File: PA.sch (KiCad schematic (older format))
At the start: 34 parts, among them IC1 CC1190

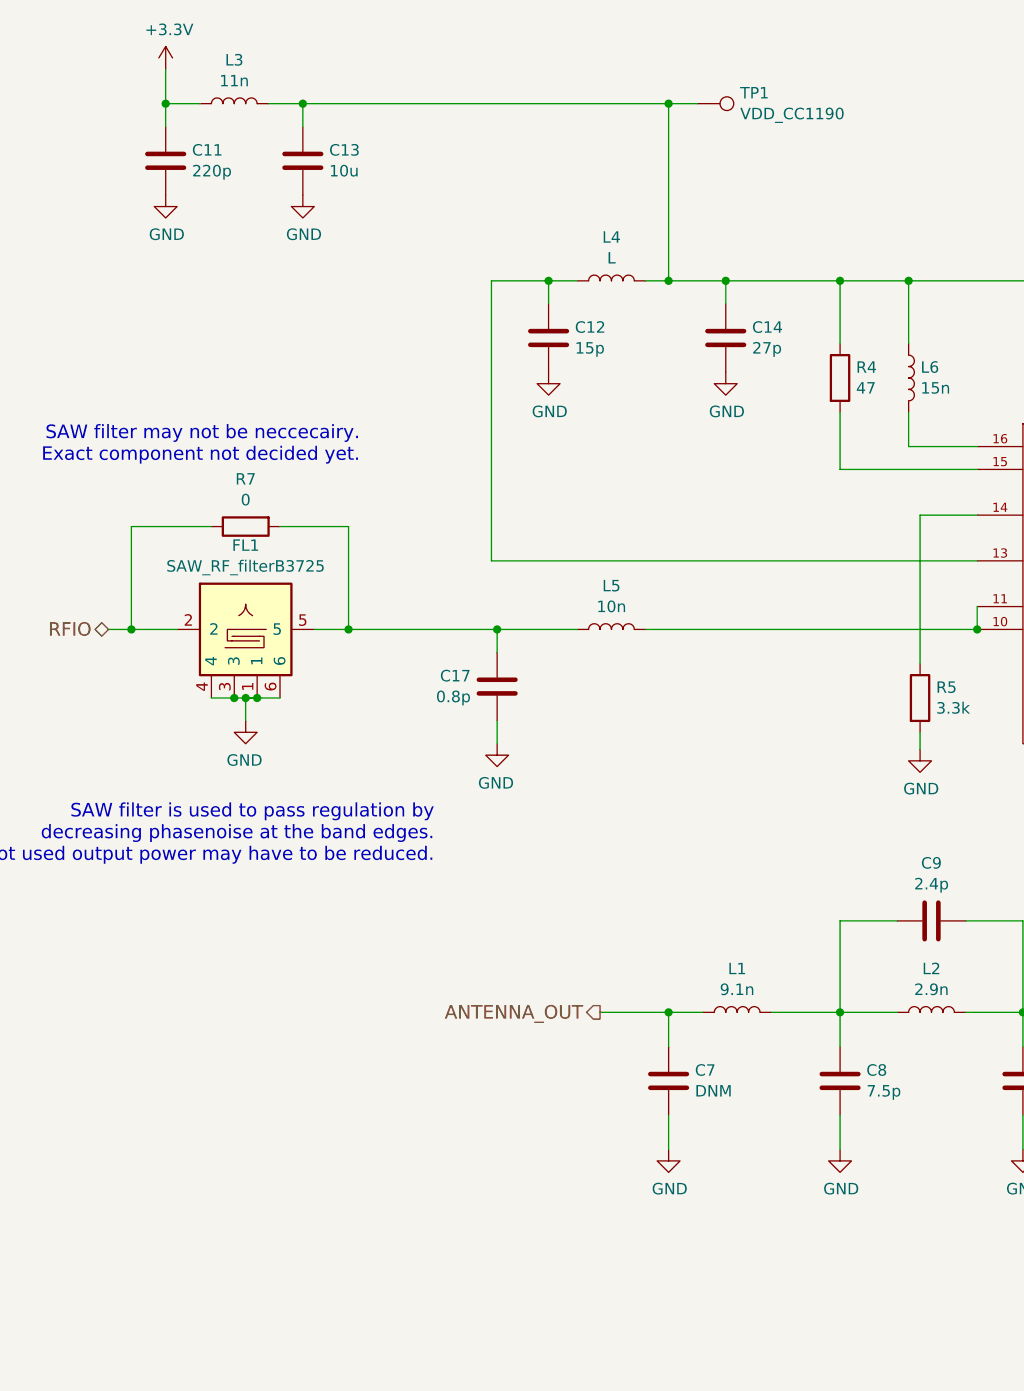
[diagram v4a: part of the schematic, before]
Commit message: Routed power for RF
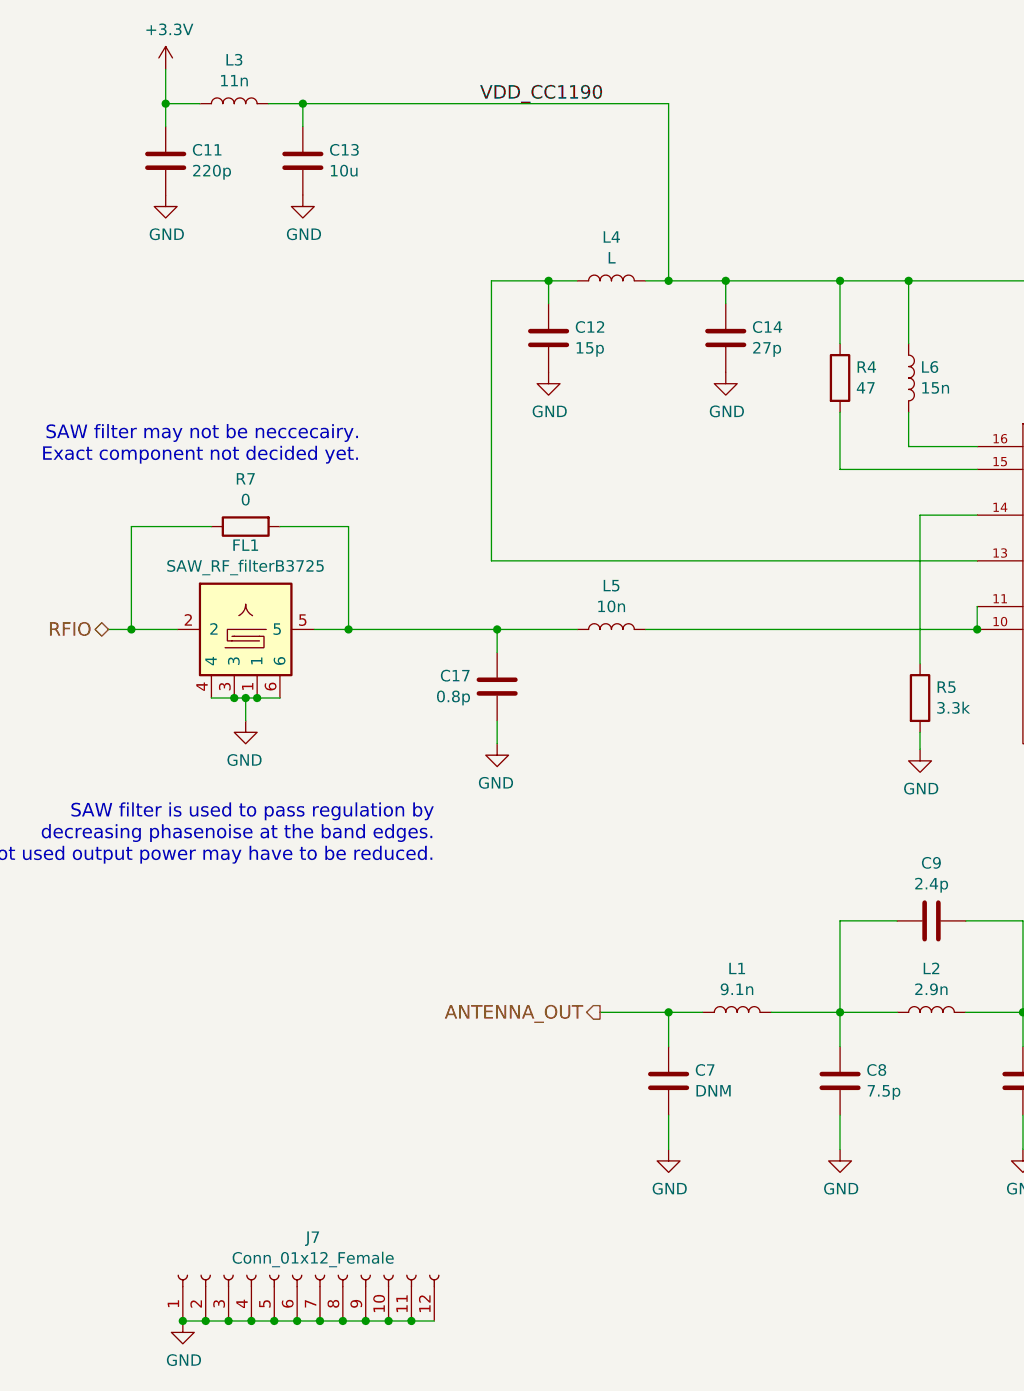
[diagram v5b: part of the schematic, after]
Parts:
- removed TP1: VDD_CC1190, TestPoint:TestPoint_Pad_2.0x2.0mm, symbol Connector:TestPoint
- added J7: Conn_01x12_Female, TU-HW RF LIB:BMIS202F, symbol Connector:Conn_01x12_Female
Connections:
- net GND: now also J7.1 (Pin_1), J7.10 (Pin_10), J7.11 (Pin_11), J7.12 (Pin_12), J7.2 (Pin_2), J7.3 (Pin_3), J7.4 (Pin_4), J7.5 (Pin_5), J7.6 (Pin_6), J7.7 (Pin_7), J7.8 (Pin_8), J7.9 (Pin_9)
- net VDD_CC1190: now reaches C13.1, C14.1, C40.1, C42.1, C43.1, L3.2, L4.2, L6.1, L8.1, R4.1
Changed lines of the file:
@@
 	6875 3700 6875 3425
-$Comp
-L Connector:TestPoint TP1
-U 1 1 601A7C22
-P 4125 975
-F 0 "TP1" V 4079 1163 50  0000 L CNN
-F 1 "VDD_CC1190" V 4170 1163 50  0000 L CNN
-F 2 "TestPoint:TestPoint_Pad_2.0x2.0mm" H 4325 975 50  0001 C CNN
-F 3 "~" H 4325 975 50  0001 C CNN
-	1    4125 975
-	0    1    1    0
-$EndComp
 $Comp
 L Device:C C11
@@
 Connection ~ 2400 975
 Wire Wire Line
-	4000 975  4125 975
-Wire Wire Line
 	4000 975  4000 1750
 Wire Wire Line
@@
 Wire Wire Line
 	2400 975  4000 975
-Connection ~ 4000 975
 Connection ~ 2150 3575
 Wire Wire Line
@@
 Wire Wire Line
 	2100 3575 2150 3575
-Wire Wire Line
-	2150 3575 2200 3575
 Connection ~ 2100 3575
 Connection ~ 2200 3575
 Wire Wire Line
 	2200 3575 2300 3575
+$Comp
+L power:GND #PWR0103
+U 1 1 602D8673
+P 1875 6300
+F 0 "#PWR0103" H 1875 6050 50  0001 C CNN
+F 1 "GND" H 1880 6127 50  0000 C CNN
+F 2 "" H 1875 6300 50  0001 C CNN
+F 3 "" H 1875 6300 50  0001 C CNN
+	1    1875 6300
+	1    0    0    -1
+$EndComp
+$Comp
+L Connector:Conn_01x12_Female J7
+U 1 1 602E7893
+P 2375 6100
+F 0 "J7" V 2540 6030 50  0000 C CNN
+F 1 "Conn_01x12_Female" V 2449 6030 50  0000 C CNN
+F 2 "TU-HW RF LIB:BMIS202F" H 2375 6100 50  0001 C CNN
+F 3 "~" H 2375 6100 50  0001 C CNN
+	1    2375 6100
+	0    -1   -1   0
+$EndComp
+Wire Wire Line
+	1875 6300 1975 6300
+Connection ~ 1875 6300
+Connection ~ 1975 6300
+Wire Wire Line
+	1975 6300 2075 6300
+Connection ~ 2075 6300
+Wire Wire Line
+	2075 6300 2175 6300
+Connection ~ 2175 6300
+Wire Wire Line
+	2175 6300 2275 6300
+Connection ~ 2275 6300
+Wire Wire Line
+	2275 6300 2375 6300
+Connection ~ 2375 6300
+Wire Wire Line
+	2375 6300 2475 6300
+Connection ~ 2475 6300
+Wire Wire Line
+	2475 6300 2575 6300
+Connection ~ 2575 6300
+Wire Wire Line
+	2575 6300 2675 6300
+Connection ~ 2675 6300
+Wire Wire Line
+	2675 6300 2775 6300
+Connection ~ 2775 6300
+Wire Wire Line
+	2775 6300 2875 6300
+Connection ~ 2875 6300
+Wire Wire Line
+	2875 6300 2975 6300
+Text Label 3175 975  0    59   ~ 0
+VDD_CC1190
 $EndSCHEMATC

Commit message: Feedback from peer review
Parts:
- removed J7: Conn_01x12_Female, TU-HW RF LIB:BMIS202F, symbol Connector:Conn_01x12_Female
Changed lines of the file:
@@
 Wire Wire Line
 	2200 3575 2300 3575
-$Comp
-L power:GND #PWR0103
-U 1 1 602D8673
-P 1875 6300
-F 0 "#PWR0103" H 1875 6050 50  0001 C CNN
-F 1 "GND" H 1880 6127 50  0000 C CNN
-F 2 "" H 1875 6300 50  0001 C CNN
-F 3 "" H 1875 6300 50  0001 C CNN
-	1    1875 6300
-	1    0    0    -1
-$EndComp
-$Comp
-L Connector:Conn_01x12_Female J7
-U 1 1 602E7893
-P 2375 6100
-F 0 "J7" V 2540 6030 50  0000 C CNN
-F 1 "Conn_01x12_Female" V 2449 6030 50  0000 C CNN
-F 2 "TU-HW RF LIB:BMIS202F" H 2375 6100 50  0001 C CNN
-F 3 "~" H 2375 6100 50  0001 C CNN
-	1    2375 6100
-	0    -1   -1   0
-$EndComp
-Wire Wire Line
-	1875 6300 1975 6300
-Connection ~ 1875 6300
-Connection ~ 1975 6300
-Wire Wire Line
-	1975 6300 2075 6300
-Connection ~ 2075 6300
-Wire Wire Line
-	2075 6300 2175 6300
-Connection ~ 2175 6300
-Wire Wire Line
-	2175 6300 2275 6300
-Connection ~ 2275 6300
-Wire Wire Line
-	2275 6300 2375 6300
-Connection ~ 2375 6300
-Wire Wire Line
-	2375 6300 2475 6300
-Connection ~ 2475 6300
-Wire Wire Line
-	2475 6300 2575 6300
-Connection ~ 2575 6300
-Wire Wire Line
-	2575 6300 2675 6300
-Connection ~ 2675 6300
-Wire Wire Line
-	2675 6300 2775 6300
-Connection ~ 2775 6300
-Wire Wire Line
-	2775 6300 2875 6300
-Connection ~ 2875 6300
-Wire Wire Line
-	2875 6300 2975 6300
 Text Label 3175 975  0    59   ~ 0
 VDD_CC1190

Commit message: Added PA shield
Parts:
- added J7: RF_Shield_One_Piece, TU-HW RF LIB:WE_shield_20x20_36503205S, symbol Device:RF_Shield_One_Piece
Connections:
- net GND: now also J7.1 (Shield)
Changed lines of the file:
@@
 Text Label 3175 975  0    59   ~ 0
 VDD_CC1190
+$Comp
+L Device:RF_Shield_One_Piece J7
+U 1 1 60330292
+P 4975 6825
+F 0 "J7" H 5605 6814 50  0000 L CNN
+F 1 "RF_Shield_One_Piece" H 5605 6723 50  0000 L CNN
+F 2 "TU-HW RF LIB:WE_shield_20x20_36503205S" H 4975 6725 50  0001 C CNN
+F 3 "~" H 4975 6725 50  0001 C CNN
+	1    4975 6825
+	1    0    0    -1
+$EndComp
+$Comp
+L power:GND #PWR0103
+U 1 1 60333F1A
+P 4975 7225
+F 0 "#PWR0103" H 4975 6975 50  0001 C CNN
+F 1 "GND" H 4980 7052 50  0000 C CNN
+F 2 "" H 4975 7225 50  0001 C CNN
+F 3 "" H 4975 7225 50  0001 C CNN
+	1    4975 7225
+	1    0    0    -1
+$EndComp
 $EndSCHEMATC

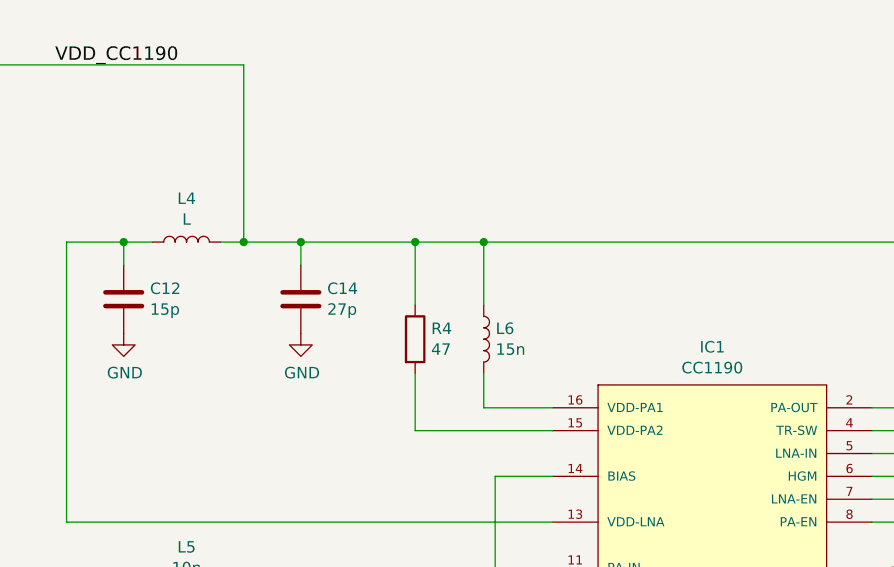
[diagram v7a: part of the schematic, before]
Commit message: Added guard ring and cleaned up silkscreen
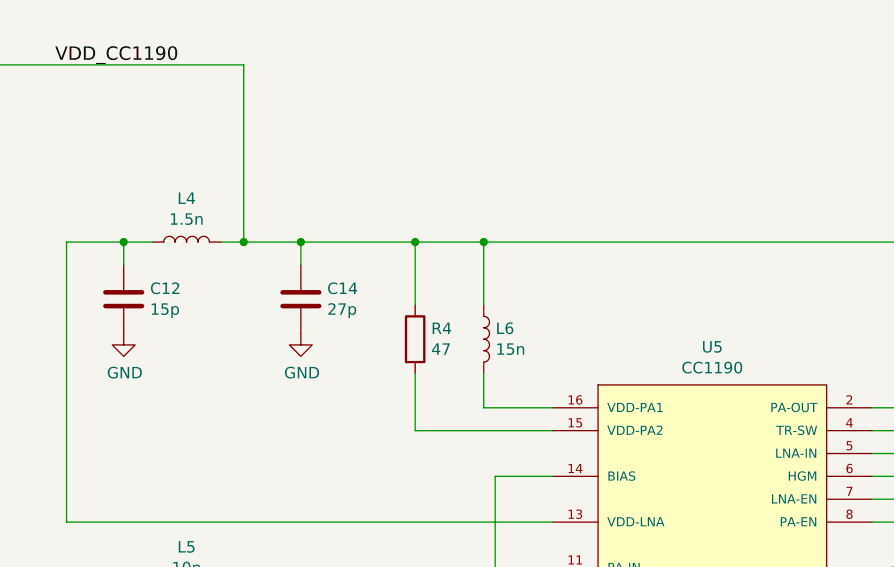
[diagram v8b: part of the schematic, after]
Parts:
- L4: value L -> 1.5n
- renumbered IC1 to U5
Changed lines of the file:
@@
 P 3750 1750
 F 0 "L4" V 3940 1750 50  0000 C CNN
-F 1 "L" V 3849 1750 50  0000 C CNN
+F 1 "1.5n" V 3849 1750 50  0000 C CNN
 F 2 "Inductor_SMD:L_0603_1608Metric" H 3750 1750 50  0001 C CNN
 F 3 "~" H 3750 1750 50  0001 C CNN
@@
 ANTENNA_OUT
 $Comp
-L KTHFS:CC1190 IC1
+L KTHFS:CC1190 U5
 U 1 1 603D6DFF
 P 6250 2775
-F 0 "IC1" H 6050 3340 50  0000 C CNN
+F 0 "U5" H 6050 3340 50  0000 C CNN
 F 1 "CC1190" H 6050 3249 50  0000 C CNN
 F 2 "Package_DFN_QFN:QFN-16-1EP_4x4mm_P0.65mm_EP2.15x2.15mm" H 5750 3375 50  0001 L BNN
